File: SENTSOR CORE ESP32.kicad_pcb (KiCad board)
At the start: 2 copper layers, 35.6 x 35.6 mm, 84 parts, among them J1 HYC80-TF08-375, J2 Conn_01x10_Pin, J3 Conn_01x10_Pin, J4 Conn_01x10_Pin, J5 JST_PH 2.0mm, J6 TYPEC-304S-ACP16, Q1 SL8205S, Q2 CJ2301, Q3 UMH3N, SW1 SW_Push, SW2 SW_Push, U1 ESP32-WROOM-32UE, U2 DS3231MZ, U3 XC6220B331MR, U4 XC6220B331MR, U5 BQ27441DRZR-G1B, U6 CN3165, U7 DW01A, U8 USBLC6-2SC6, U9 CH340K

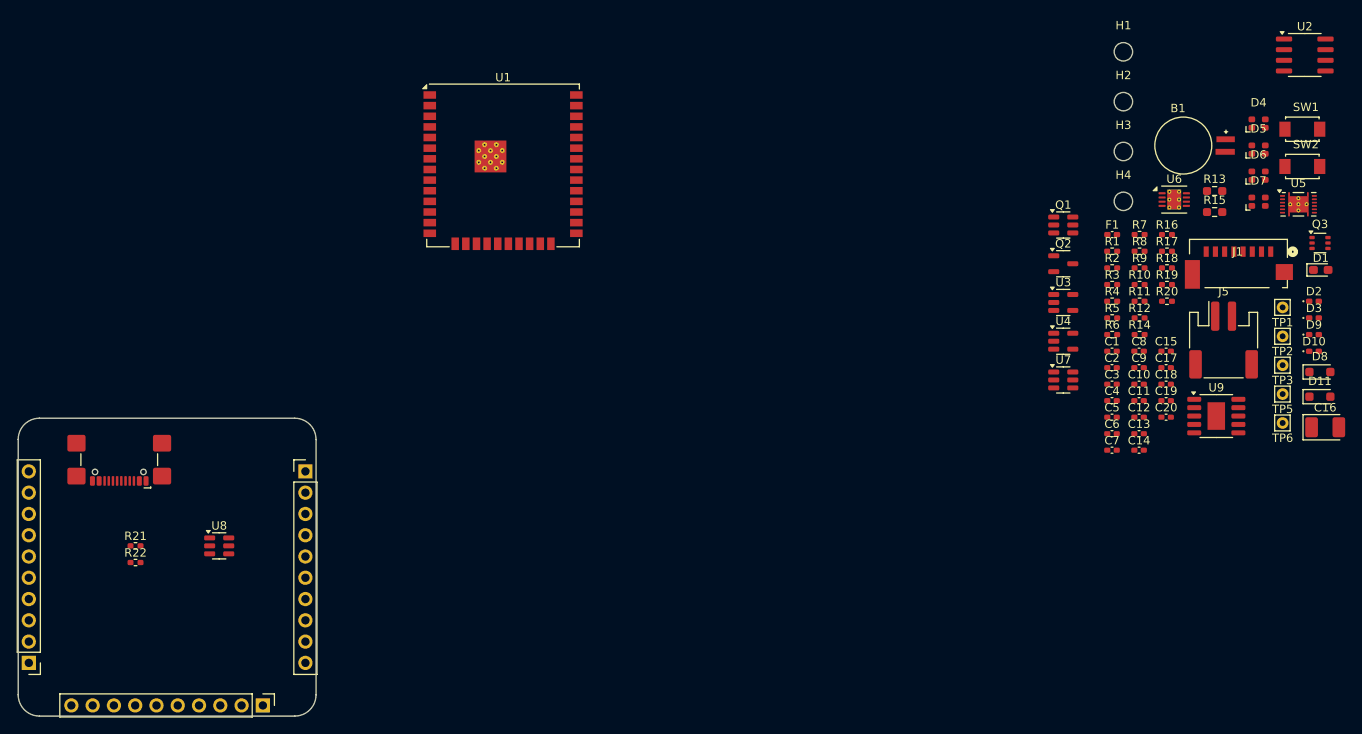
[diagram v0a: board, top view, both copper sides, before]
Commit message: add board cut line
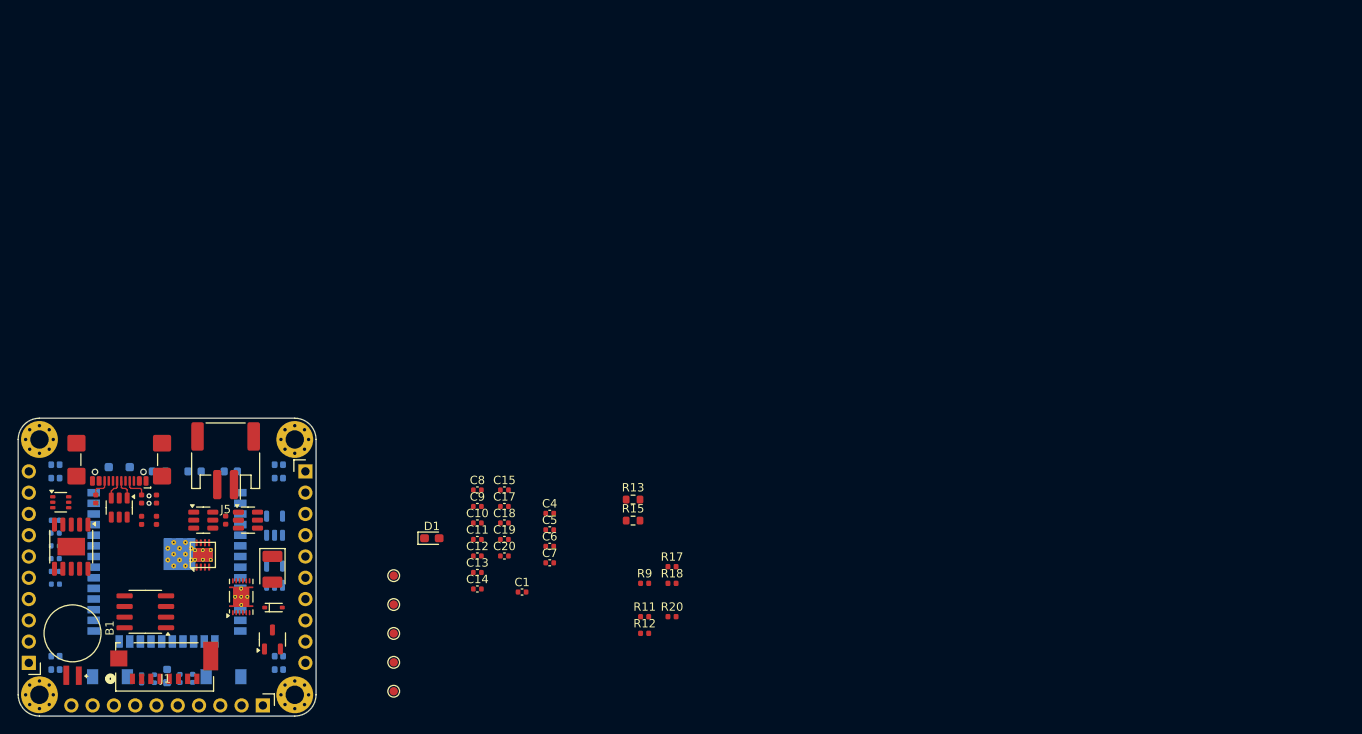
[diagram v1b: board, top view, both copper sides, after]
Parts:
- removed C2: 100nF, Capacitor_SMD:C_0402_1005Metric_Pad0.74x0.62mm_HandSolder
- C1, C10, C11, C12, C13, C14, C15, C17, C18, C19, C20, C4, C5, C6, C7, C8, C9: footprint Capacitor_SMD:C_0402_1005Metric_Pad0.74x0.62mm_HandSolder -> Capacitor_SMD:C_0402_1005Metric
- C16: footprint Capacitor_Tantalum_SMD:CP_EIA-3528-12_Kemet-T_HandSolder -> Capacitor_Tantalum_SMD:CP_EIA-3528-12_Kemet-T
- C3: footprint Capacitor_SMD:C_0402_1005Metric_Pad0.74x0.62mm_HandSolder -> Capacitor_SMD:C_0402_1005Metric; moved to B.Cu
- D10, D2, D3, D9: footprint LED_SMD:LED_0402_1005Metric_Pad0.77x0.64mm_HandSolder -> LED_SMD:LED_0603_1608Metric; moved to B.Cu
- D11, D4, D5, D6, D7, SW1, SW2, U1, U3, U4: moved to B.Cu
- D8: footprint Diode_SMD:D_SOD-323_HandSoldering -> Diode_SMD:D_SOD-323
- F1: footprint Fuse:Fuse_0402_1005Metric_Pad0.77x0.64mm_HandSolder -> Fuse:Fuse_0402_1005Metric
- H1, H2, H3, H4: footprint MountingHole:MountingHole_2.2mm_M2 -> MountingHole:MountingHole_2.2mm_M2_Pad_Via
- R1, R16, R2, R3, R4, R5, R6, R7, R8: footprint Resistor_SMD:R_0402_1005Metric_Pad0.72x0.64mm_HandSolder -> Fuse:Fuse_0402_1005Metric; moved to B.Cu
- R10, R11, R12, R14, R17, R18, R19, R20, R21, R22, R9: footprint Resistor_SMD:R_0402_1005Metric_Pad0.72x0.64mm_HandSolder -> Fuse:Fuse_0402_1005Metric
- R13, R15: footprint Resistor_SMD:R_0603_1608Metric_Pad0.98x0.95mm_HandSolder -> Resistor_SMD:R_0603_1608Metric
- TP1, TP2, TP3, TP5, TP6: footprint Connector_Pin:Pin_D0.7mm_L6.5mm_W1.8mm_FlatFork -> TestPoint:TestPoint_Pad_D1.0mm
- moved D4 157.4 mm to (94.3, 124.1), turned to 90 degrees
- moved SW2 154.8 mm to (100.8, 125.8)
- moved U2 153.5 mm to (105.0, 118.0), turned to 180 degrees
- moved Q3 153.5 mm to (94.9, 105.0)
- moved H1 150.5 mm to (92.4, 127.9)
- moved D5 148.7 mm to (94.3, 101.3), turned to -90 degrees
- moved B1 144.8 mm to (96.3, 120.6), turned to -90 degrees
- moved SW1 144.4 mm to (114.4, 125.8), turned to 180 degrees
- moved D11 143.6 mm to (101.9, 100.8), turned to 180 degrees
- moved D3 143.4 mm to (107.6, 125.7), turned to -90 degrees
- moved D2 139.4 mm to (106.6, 101.3)
- moved U9 137.6 mm to (96.2, 110.3), turned to -90 degrees
- moved J1 136.9 mm to (107.3, 124.6), turned to 180 degrees
- moved R7 135.6 mm to (94.3, 113.2)
- moved U5 134.6 mm to (116.5, 116.2), turned to 90 degrees
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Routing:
- net /D_P: track 0.00 -> 3.09 mm
- net /D_N: track 0.00 -> 3.02 mm
- net Net-(J6-CC1): track 0.00 -> 3.00 mm
- net Net-(J6-CC2): track 0.00 -> 2.62 mm
- net GND: vias 0 -> 2
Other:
- board text removed: "Conn_01x10_Pin"

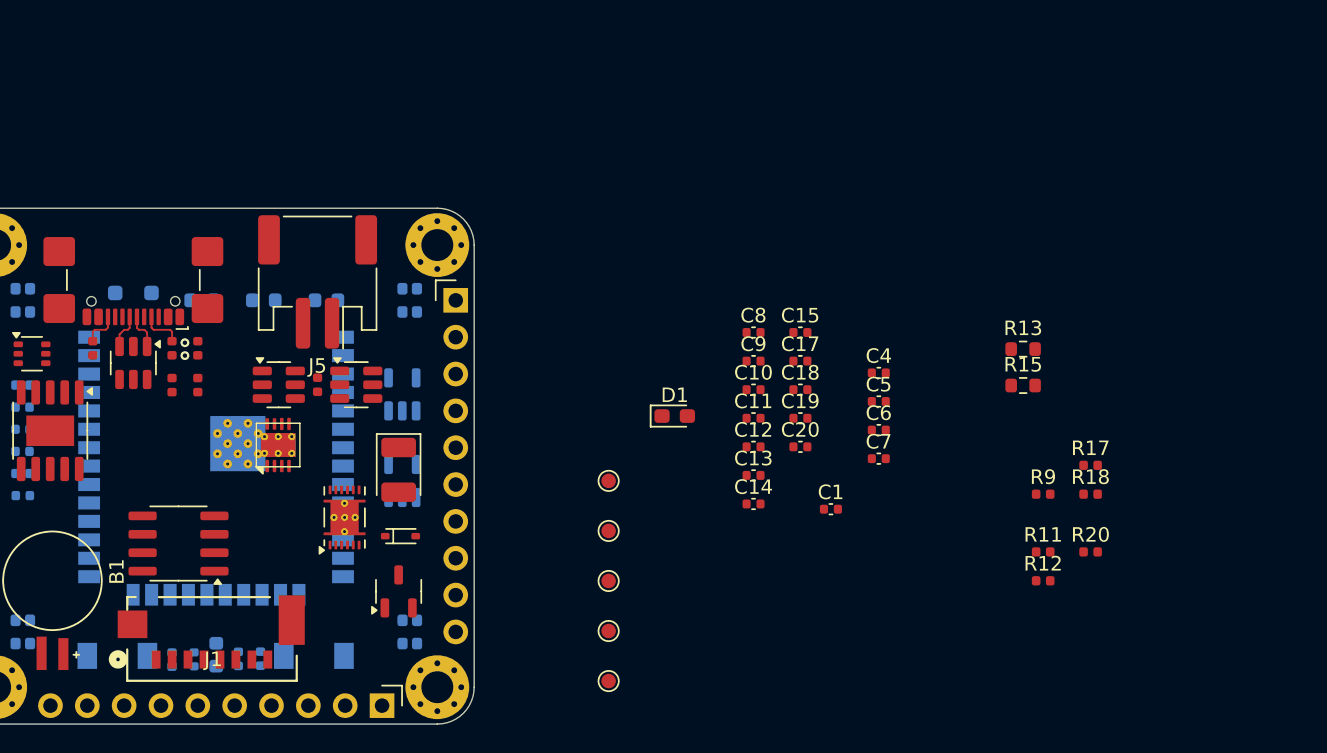
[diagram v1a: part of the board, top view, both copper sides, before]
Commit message: add board cut line
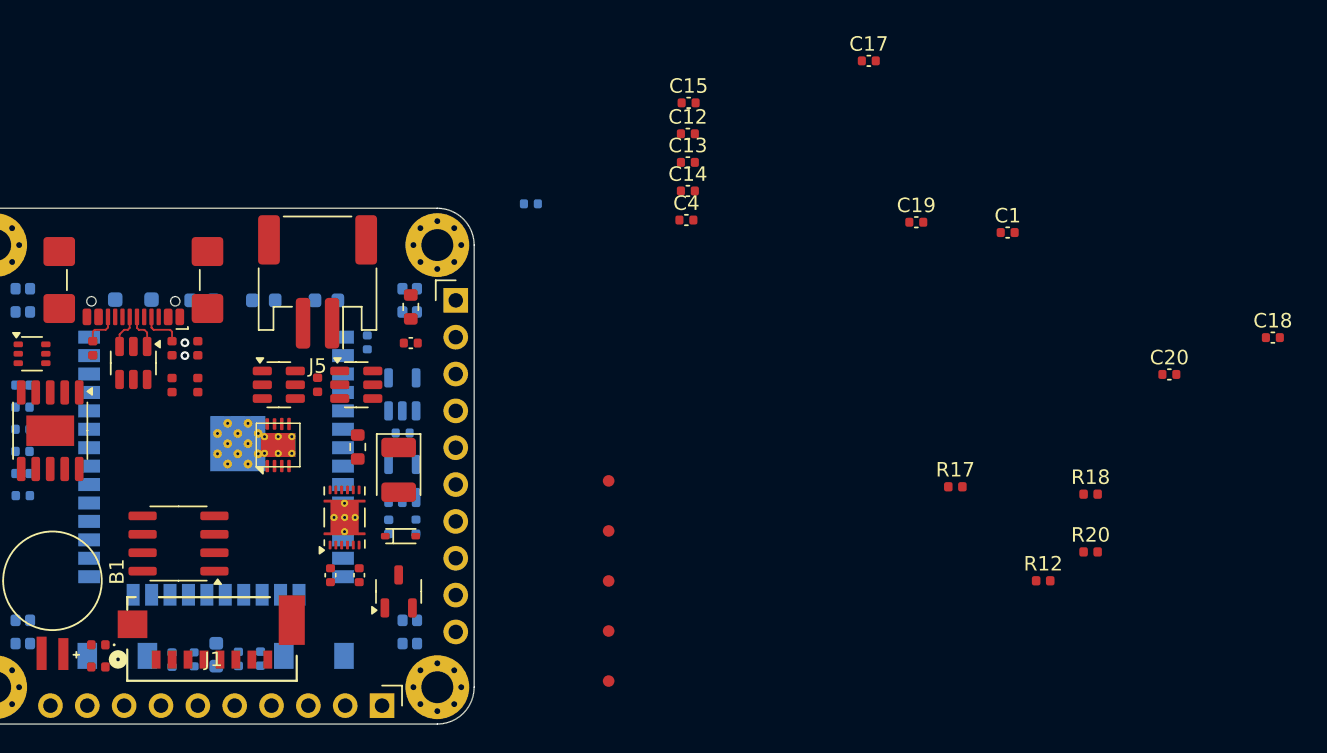
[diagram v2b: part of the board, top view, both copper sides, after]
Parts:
- C5, C6, C7, C8, R11: moved to B.Cu
- D1: footprint Diode_SMD:D_0603_1608Metric_Pad1.05x0.95mm_HandSolder -> Diode_SMD:D_0402_1005Metric
- moved R9 66.2 mm to (99.5, 126.5)
- moved R13 46.4 mm to (117.4, 111.4), turned to -90 degrees
- moved R11 45.2 mm to (119.5, 116.9), turned to -90 degrees
- moved D1 42.8 mm to (99.5, 125.0), turned to 180 degrees
- moved R15 42.6 mm to (121.0, 101.7), turned to -90 degrees
- moved C6 35.8 mm to (118.0, 104.2), turned to -90 degrees
- moved C5 32.9 mm to (120.5, 110.4)
- moved C18 32.8 mm to (180.5, 103.8)
- moved C9 32.7 mm to (115.5, 120.2), turned to 90 degrees
- moved C7 32.3 mm to (121.4, 116.9), turned to 90 degrees
- moved C10 30.0 mm to (117.5, 120.2), turned to 90 degrees
- moved C20 25.9 mm to (173.3, 106.4)
- moved C11 24.2 mm to (121.0, 104.2), turned to 180 degrees
- moved C1 22.6 mm to (162.2, 96.6)
- moved C12 22.0 mm to (140.1, 89.8)
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
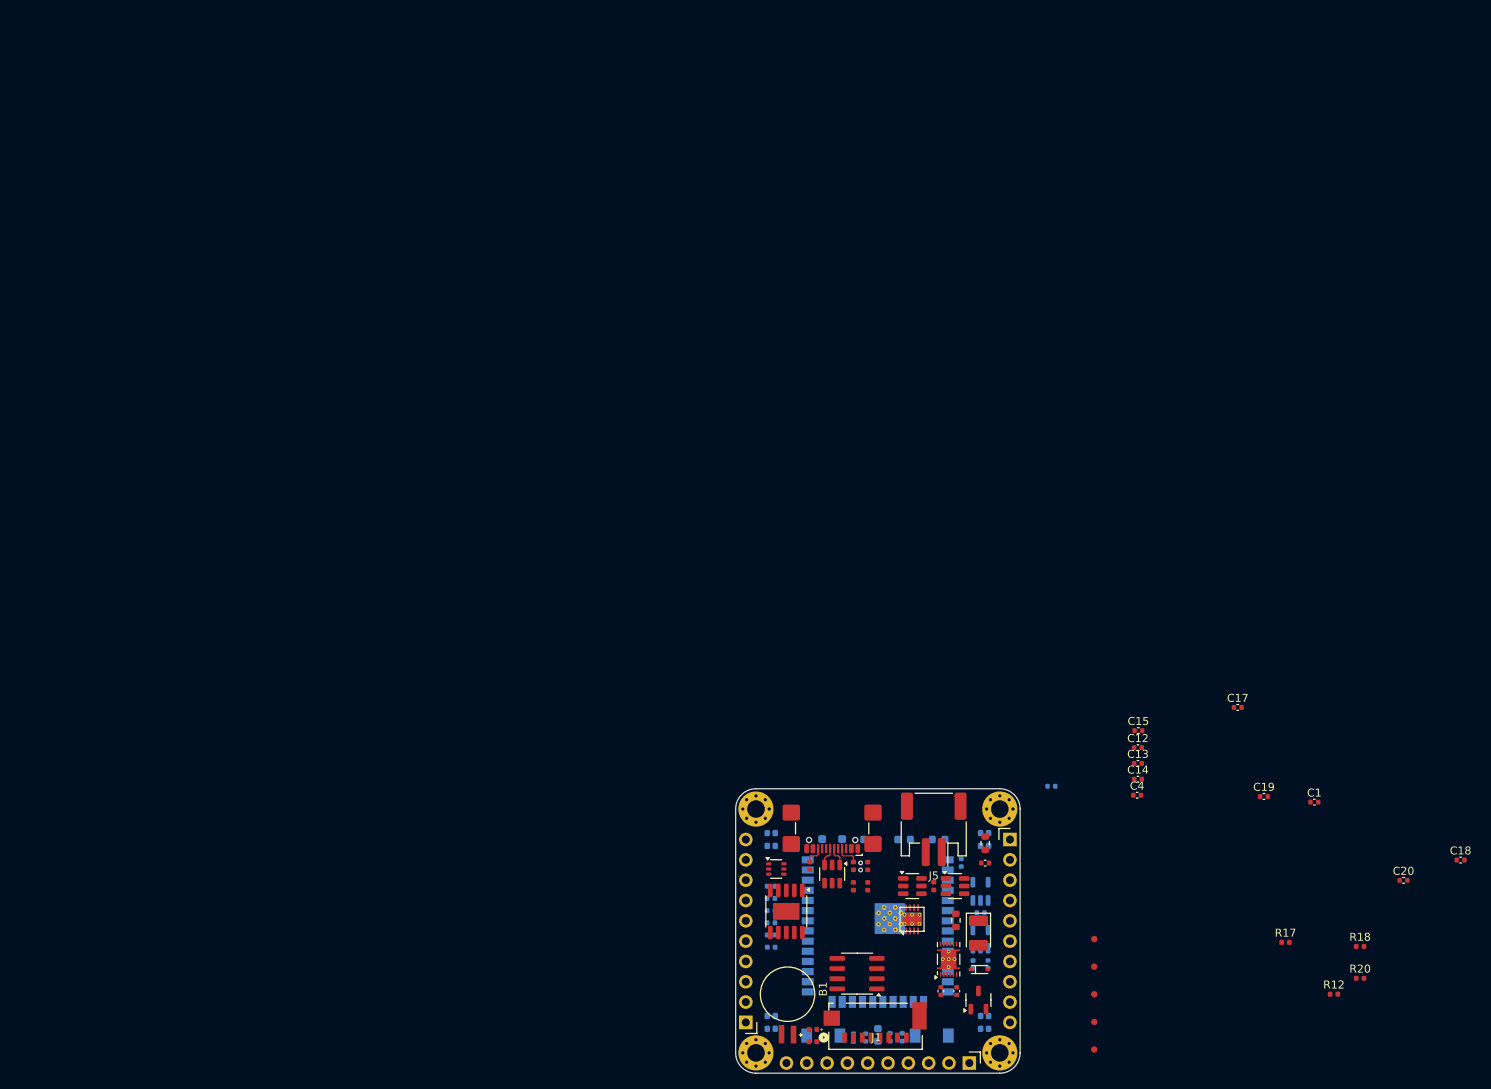
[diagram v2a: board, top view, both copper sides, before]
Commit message: add board layout
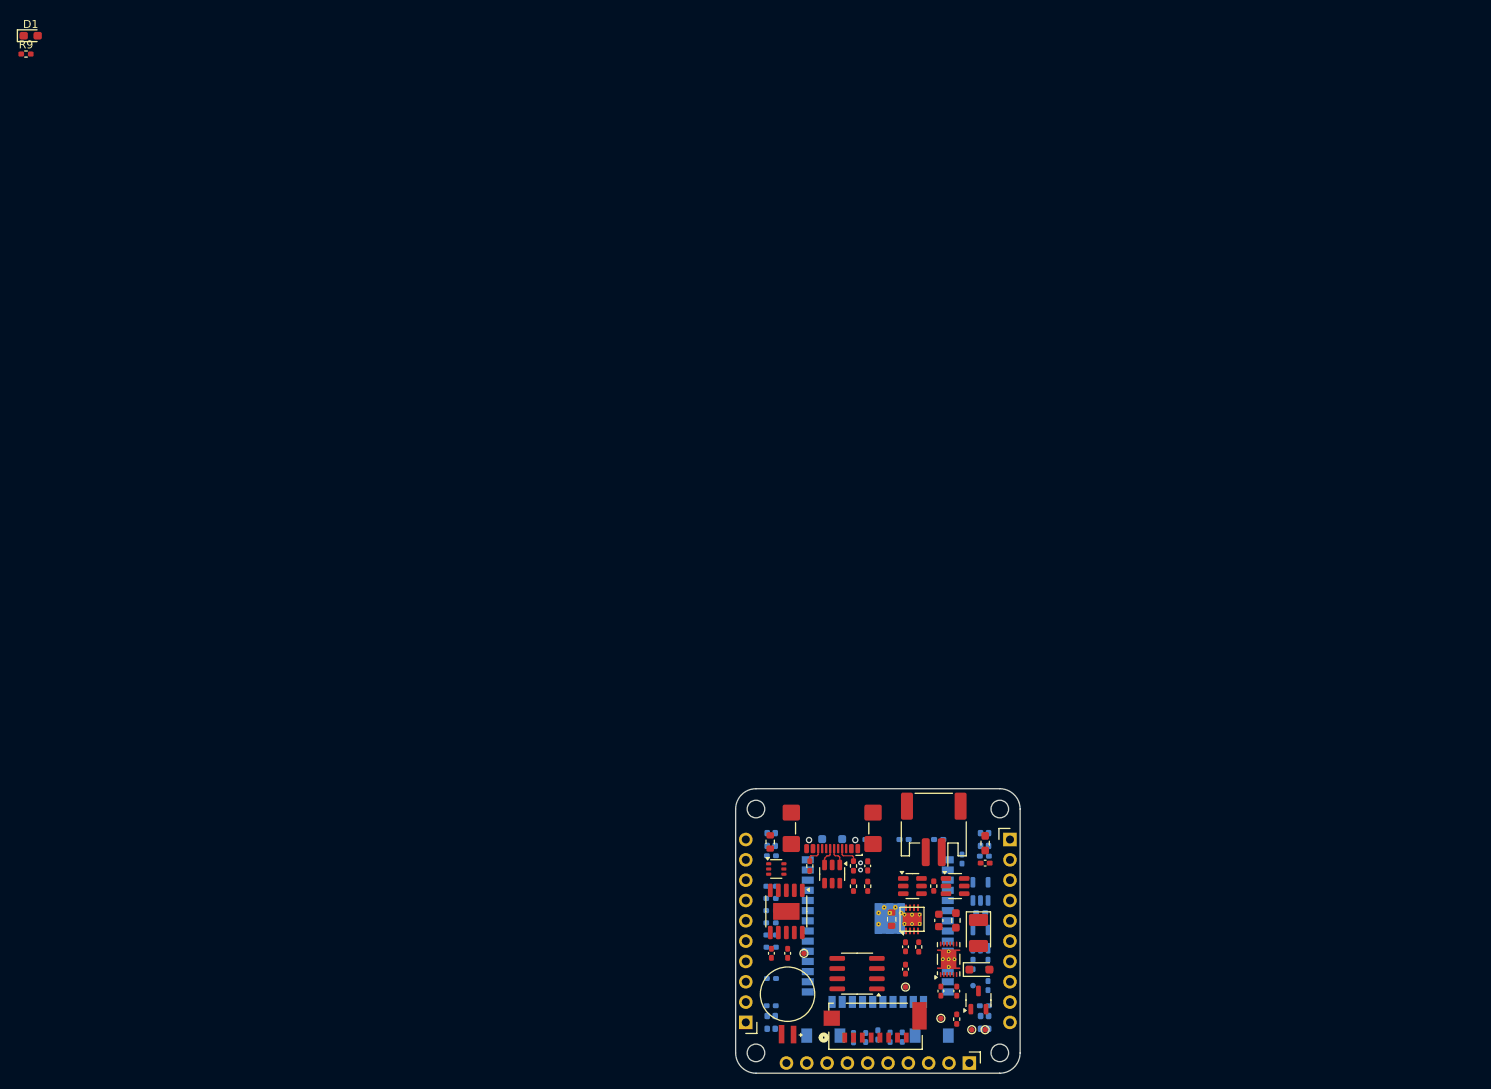
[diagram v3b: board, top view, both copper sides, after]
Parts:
- added TP4: 32K, lib:TestPoint_Pad_D0.7mm, F.Cu at (111.1, 119.7)
- C1, C12, C13, C14, C15: footprint Capacitor_SMD:C_0402_1005Metric -> Capacitor_SMD:C_0402_1005Metric_Pad0.74x0.62mm_HandSolder; moved to B.Cu
- C10, C11, C18, C19, C20, C3, C4, C5, C6, C7, C8, C9: footprint Capacitor_SMD:C_0402_1005Metric -> Capacitor_SMD:C_0402_1005Metric_Pad0.74x0.62mm_HandSolder
- C16: footprint Capacitor_Tantalum_SMD:CP_EIA-3528-12_Kemet-T -> Capacitor_Tantalum_SMD:CP_EIA-3528-12_Kemet-T_HandSolder
- C17: footprint Capacitor_SMD:C_0402_1005Metric -> Capacitor_SMD:C_0603_1608Metric
- D1: footprint Diode_SMD:D_0402_1005Metric -> Diode_SMD:D_0603_1608Metric_Pad1.05x0.95mm_HandSolder
- D10, D2, D3, D9: footprint LED_SMD:LED_0603_1608Metric -> LED_SMD:LED_0402_1005Metric_Pad0.77x0.64mm_HandSolder
- D8: footprint Diode_SMD:D_SOD-323 -> Diode_SMD:D_SOD-323_HandSoldering
- F1: footprint Fuse:Fuse_0402_1005Metric -> Fuse:Fuse_0402_1005Metric_Pad0.77x0.64mm_HandSolder
- H1, H2, H3, H4: footprint MountingHole:MountingHole_2.2mm_M2_Pad_Via -> MountingHole:MountingHole_2.2mm_M2
- R1, R10, R11, R14, R16, R17, R19, R2, R21, R22, R3, R4, R5, R6, R7, R8, R9: footprint Fuse:Fuse_0402_1005Metric -> Resistor_SMD:R_0402_1005Metric_Pad0.72x0.64mm_HandSolder
- R12: value 1k -> 10k; footprint Fuse:Fuse_0402_1005Metric -> Resistor_SMD:R_0402_1005Metric_Pad0.72x0.64mm_HandSolder
- R13, R15: footprint Resistor_SMD:R_0603_1608Metric -> Resistor_SMD:R_0603_1608Metric_Pad0.98x0.95mm_HandSolder
- R18, R20: footprint Fuse:Fuse_0402_1005Metric -> Resistor_SMD:R_0603_1608Metric
- TP1, TP3: footprint TestPoint:TestPoint_Pad_D1.0mm -> lib:TestPoint_Pad_D0.7mm
- TP2: footprint TestPoint:TestPoint_Pad_D1.0mm -> lib:TestPoint_Pad_D0.7mm; moved to B.Cu
- TP5: value RGB_DOUT -> VIN; footprint TestPoint:TestPoint_Pad_D1.0mm -> lib:TestPoint_Pad_D0.7mm
- TP6: value RGB_DOUT -> GND; footprint TestPoint:TestPoint_Pad_D1.0mm -> lib:TestPoint_Pad_D0.7mm
- moved D1 158.1 mm to (1.72, 0.80), turned to 0 degrees
- moved R9 157.8 mm to (1.14, 3.08)
- moved C20 79.5 mm to (94.3, 115.5), turned to 90 degrees
- moved R20 75.7 mm to (94.2, 101.6), turned to 90 degrees
- moved C18 70.2 mm to (111.1, 114.7), turned to -90 degrees
- moved C19 62.7 mm to (96.3, 115.5), turned to -90 degrees
- moved R18 58.6 mm to (109.3, 111.2), turned to 90 degrees
- moved C13 54.9 mm to (94.3, 122.0), turned to 180 degrees
- moved R12 52.2 mm to (112.7, 114.7), turned to 90 degrees
- moved C15 48.5 mm to (94.3, 103.3), turned to 180 degrees
- moved C1 46.8 mm to (121.4, 119.5), turned to 90 degrees
- moved C17 45.9 mm to (115.2, 111.4), turned to 90 degrees
- moved R17 42.2 mm to (117.5, 123.7), turned to -90 degrees
- moved TP1 36.3 mm to (98.4, 115.5)
- moved C4 36.2 mm to (111.1, 117.5), turned to -90 degrees
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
